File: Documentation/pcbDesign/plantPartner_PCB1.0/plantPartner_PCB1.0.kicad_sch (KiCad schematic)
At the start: 53 parts, among them IC1 MPM3610, J1 Conn_01x04, J10 Screw_Terminal, J2 Conn_01x04, J3 Conn_01x04, J4 Screw_Terminal, J5 Screw_Terminal, J6 Screw_Terminal, J7 Conn_01x03, J8 Screw_Terminal, J9 Conn_01x03, K1 SRD-05VDC-SL-C, K2 SRD-05VDC-SL-C, Q1 PNP, Q2 PNP, U1 ESP32-WROOM-32, U2 MAX485, U3 ESP32-DEVKIT-V1

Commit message: Put in the correct ESP32 (DEVKIT-V1) into Schematic. Updated the IO pin connections for ESP. Added Power supply system to SChematic. Need to update optocoupler symbol and footprint. Then routing shall commence
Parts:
- removed R22: 1k, Resistor_SMD:R_0201_0603Metric, symbol Device:R
- removed U1: ESP32-WROOM-32, RF_Module:ESP32-WROOM-32, symbol RF_Module:ESP32-WROOM-32
- added D8, D9: SS14, Diode_SMD:D_SMA, symbol Device:D_Schottky
- added J11, J16: Conn_01x04, Connector_PinHeader_2.54mm:PinHeader_1x04_P2.54mm_Vertical, symbol Connector_Generic:Conn_01x04
- added J12, J13, J14, J15: Conn_01x03, Connector_PinHeader_2.54mm:PinHeader_1x03_P2.54mm_Vertical, symbol Connector_Generic:Conn_01x03
- added J17: Barrel_Jack, Connector_BarrelJack:BarrelJack_GCT_DCJ200-10-A_Horizontal, symbol Connector:Barrel_Jack_MountingPin
- added J18: Screw_Terminal_01x02, TerminalBlock_Phoenix:TerminalBlock_Phoenix_MKDS-1,5-2-5.08_1x02_P5.08mm_Horizontal, symbol Connector:Screw_Terminal_01x02
- added R23: 1k, Resistor_SMD:R_0201_0603Metric, symbol Device:R
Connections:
- net VCC is gone; now on net 12V: IC1.2 (VCC)
- net 12V: now also U3.30 (VIN), D8.1 (K), D9.1 (K), J11.3 (Pin_3), J12.1 (Pin_1), J14.1 (Pin_1), J16.2 (Pin_2), J16.3 (Pin_3)
- net A: now also J11.2 (Pin_2)
- net ADC_LIGHT_SENSOR: now also U3.17 (VP)
- net ADC_MOISTURE_SENSOR: now also U3.18 (VN)
- net B: now also J11.1 (Pin_1)
- net COM: now also J13.2 (Pin_2), J15.2 (Pin_2)
- net DC+: now also J12.3 (Pin_3), J14.3 (Pin_3)
- net DE: now also U3.11 (D21)
- net DI: now also U3.7 (TX2)
- net EN: now also J16.4 (Pin_4)
- net FB: now also J16.1 (Pin_1)
- net GND: now also J11.4 (Pin_4), J12.2 (Pin_2), J14.2 (Pin_2), J17.2, J18.2 (Pin_2)
- net NC: now also J13.3 (Pin_3), J15.3 (Pin_3)
- net NO: now also J13.1 (Pin_1), J15.1 (Pin_1)
- net PWM_FERTIL_PIN: now also U3.28 (D13)
- net PWM_WATER_PIN: now also U3.27 (D12)
- net RO: now also R23.2
- net TEMP SWITCH: now reaches U3.20 (D35)
- net EXTERNAL LED: now reaches U3.26 (D14)
- net INTERNAL LED: now reaches U3.4 (D2)
- net at U3.6 (RX2): now also R23.1
- new net 12V_JACK: D8.2 (A), J17.1
- new net 12V_SCREW: D9.2 (A), J18.1 (Pin_1)
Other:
- note added: "ESP-32 WROOM DEVKIT V1"
- note added: "Finish testing pins for ESP32 with labels for what each Pin does. Have a stack for pins that we use and other for ones we do not."
- note added: "Power Supplies"
- note removed: "ESP-32 WROOM"
- moved on the sheet: U3

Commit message: Added the small circuitry needed for ADC sensors, ESP-32 External LED, Overall PCB Heartbeat sensor. Fixed wiring issue with 5V Relays. Met with Prof. Alex about our Alpha Build status. I tried to add new optocoupler symbol and footprint but KiCad could not find it for some reason (rip). Now I need to add used ESP-32 pins, extra 5V and 12V pins, extra GND pins, and unused ESP32 Pins, THEN finally I can route (I hope … please lol).
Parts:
- removed J17: Barrel_Jack, Connector_BarrelJack:BarrelJack_GCT_DCJ200-10-A_Horizontal, symbol Connector:Barrel_Jack_MountingPin
- removed J5, J8: Screw_Terminal, TerminalBlock_Phoenix:TerminalBlock_Phoenix_MKDS-1,5-3-5.08_1x03_P5.08mm_Horizontal, symbol Connector:Screw_Terminal_01x03
- added D10: LED, LED_SMD:LED_0201_0603Metric, symbol Device:LED
- added D11: LED, symbol Device:LED
- added J17: Conn_01x03, symbol Connector_Generic:Conn_01x03
- added J19: Barrel_Jack, Connector_BarrelJack:BarrelJack_GCT_DCJ200-10-A_Horizontal, symbol Connector:Barrel_Jack
- added J5: Conn_01x02, symbol Connector_Generic:Conn_01x02
- added R22, R24, R26: 1k, Resistor_SMD:R_0201_0603Metric, symbol Device:R
- J10, J6: value Screw_Terminal -> Screw_Terminal_01x03; footprint TerminalBlock_Phoenix:TerminalBlock_Phoenix_MKDS-1,5-3-5.08_1x03_P5.08mm_Horizontal -> (none)
- U3: footprint ESP32-DEVKIT-V1:MODULE_ESP32_DEVKIT_V1 -> MyCustomFootprints:MODULE_ESP32_DEVKIT_V1
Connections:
- net DC+ is gone; now on net 12V: J12.3 (Pin_3), J14.3 (Pin_3), J7.3 (Pin_3), J9.3 (Pin_3), Q1.3 (E), Q2.3 (E), R12.1, R14.1, R17.1, R19.1
- net PWM_FERTIL_PIN is gone; now on net 12V: U3.28 (D13)
- net PWM_WATER_PIN is gone; now on net 12V: U3.27 (D12)
- net 12V: now also J13.3 (Pin_3), J15.3 (Pin_3), K1.NC, K2.NC, J17.2 (Pin_2), J5.2 (Pin_2), R26.1
- net 12V_JACK: now also J19.1
- net ADC_LIGHT_SENSOR: now also J5.1 (Pin_1), R24.1
- net ADC_MOISTURE_SENSOR: now also J17.3 (Pin_3)
- net COM: now also J10.3 (Pin_3), J6.3 (Pin_3); no longer J10.2 (Pin_2), J6.2 (Pin_2)
- net EXTERNAL LED: now also R22.2
- net GND: now also J10.1 (Pin_1), J6.1 (Pin_1), D10.1 (K), D11.1 (K), J17.1 (Pin_1), J19.2, R24.2
- net NO: now also J10.2 (Pin_2), J6.2 (Pin_2); no longer J10.1 (Pin_1), J6.1 (Pin_1)
- removed net NC: J10.3 (Pin_3), J13.3 (Pin_3), J15.3 (Pin_3), J6.3 (Pin_3), K1.NC, K2.NC
- new net: D10.2 (A), R22.1
- new net: D11.2 (A), R26.2
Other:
- note added: "5V Relay - Fertilizer Pump"
- note added: "5V Relay - Water Pump"
- note added: "Assign Footprints to necessary LEDs/Diodes and Screw Terminals"
- note added: "Heartbeat LED"
- note added: "Pins to Add: Several 12V, 5V, and GND pins; ESP-32 Pins we are using for sensors ESP-32 Pins we are NOT using for sensors and their potential usages"
- note added: "Route PCB"
- note removed: "5V Relay - 1 of 2"
- note removed: "5V Relay - 2 of 2"
- note removed: "Verify that the imported OPTO_EL357N-G is equal to the EL354 that I have been assuming. Import all the 3D models accordingly after, add testing pins on Schematic, route PCB and add any necessary text to it"
- moved on the sheet: D8, D9, J12, J13, J14, J15, J18, R23, U3

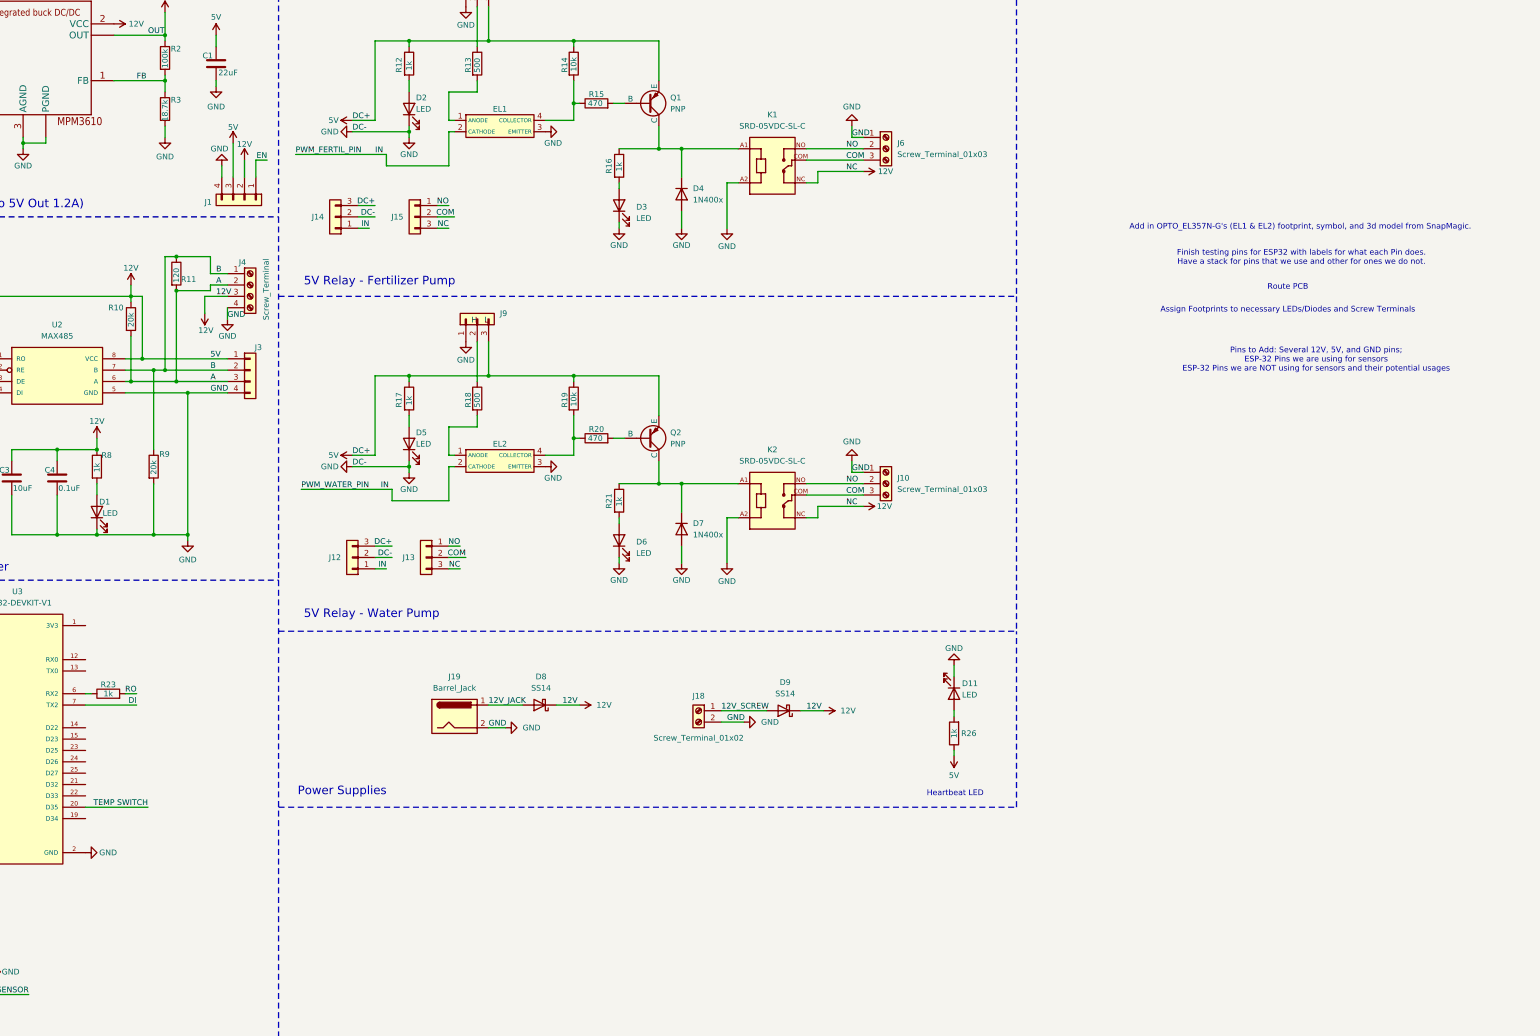
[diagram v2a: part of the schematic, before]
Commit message: Fixed optocoupler for Relay circuits
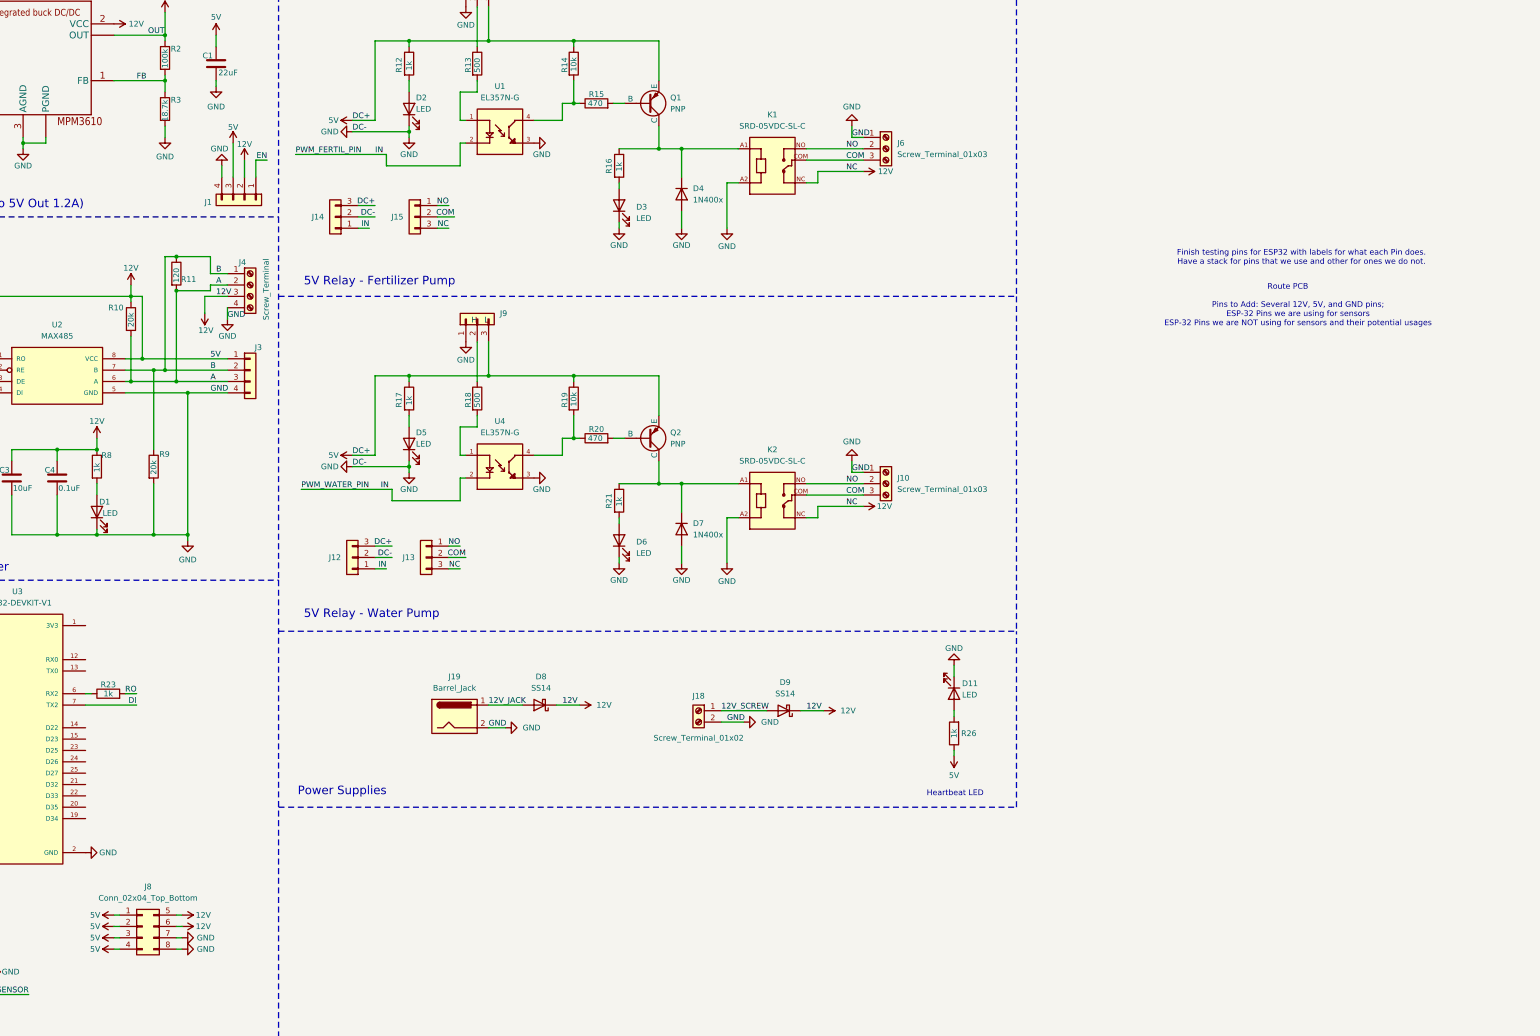
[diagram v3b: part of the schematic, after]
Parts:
- removed EL1, EL2: ~, MyCustomFootprints:OPTO_EL357N-G, symbol 12V_Relay:EL354(TA)
- added J8: Conn_02x04_Top_Bottom, Connector_PinHeader_2.54mm:PinHeader_2x04_P2.54mm_Vertical, symbol Connector_Generic:Conn_02x04_Top_Bottom
- added U1, U4: EL357N-G, MyCustomFootprints:OPTO_EL357N-G, symbol EL357N-G:EL357N-G
- D11: footprint (none) -> LED_SMD:LED_0201_0603Metric
- J10, J6: footprint (none) -> TerminalBlock_Phoenix:TerminalBlock_Phoenix_MKDS-1,5-3-5.08_1x03_P5.08mm_Horizontal
- J17: footprint (none) -> Connector_PinHeader_2.54mm:PinHeader_1x03_P2.54mm_Vertical
- J5: footprint (none) -> Connector_PinHeader_2.54mm:PinHeader_1x02_P2.54mm_Vertical
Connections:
- net 12V: now also J8.1 (Pin_1), J8.2 (Pin_2), J8.3 (Pin_3), J8.4 (Pin_4), J8.5 (Pin_5), J8.6 (Pin_6), U1.2, U4.2
- net GND: now also J8.7 (Pin_7), J8.8 (Pin_8), U1.3, U4.3
- net at R13.2: now also U1.1
- net at R14.2, R15.1: now also U1.4
- net at R19.2, R20.1: now also U4.4
- net at R18.2: now also U4.1
- net TEMP SWITCH: no longer names the net of U3.20 (D35)
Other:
- note removed: "Add in OPTO_EL357N-G's (EL1 & EL2) footprint, symbol, and 3d model from SnapMagic."
- note removed: "Assign Footprints to necessary LEDs/Diodes and Screw Terminals"

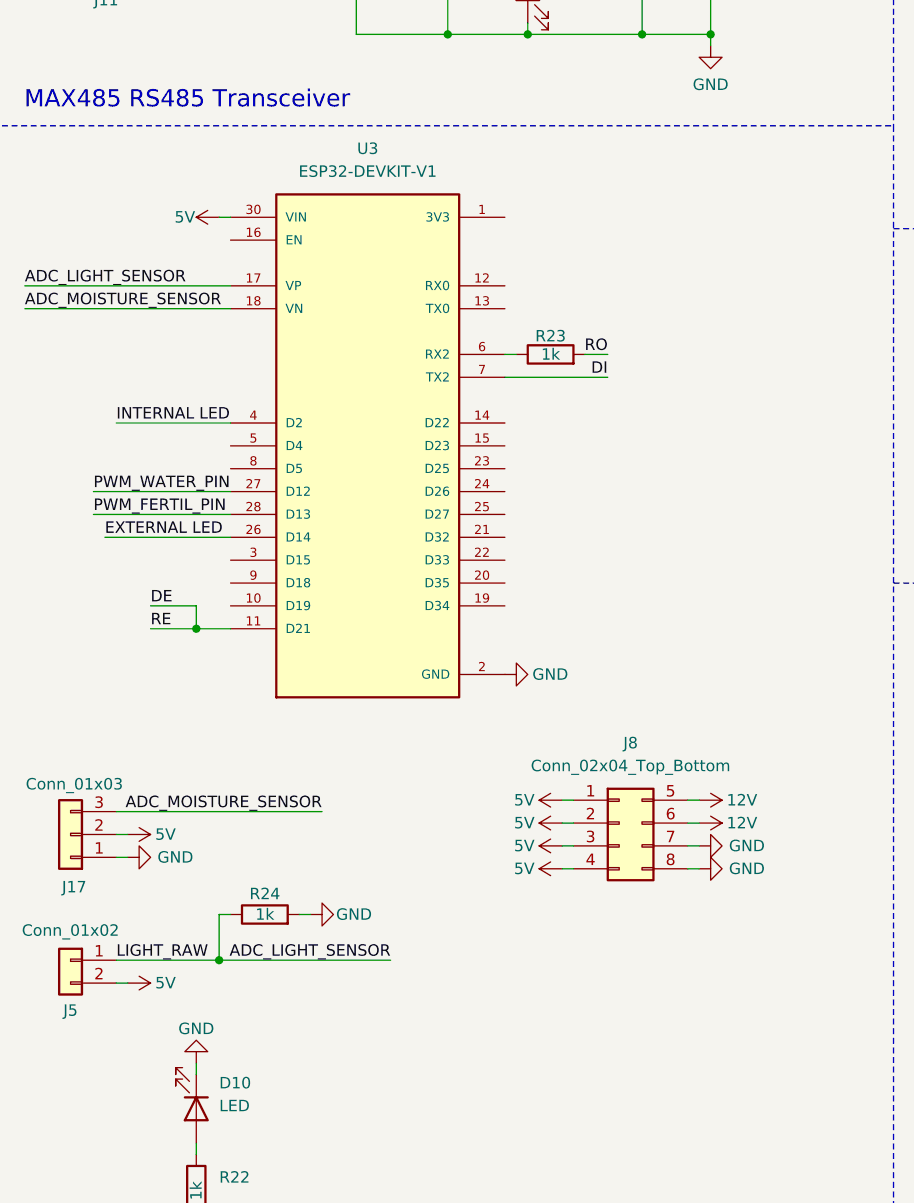
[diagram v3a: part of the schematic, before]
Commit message: Added Labels to majority of unused ESP32 Pins. I will fill in the rest later
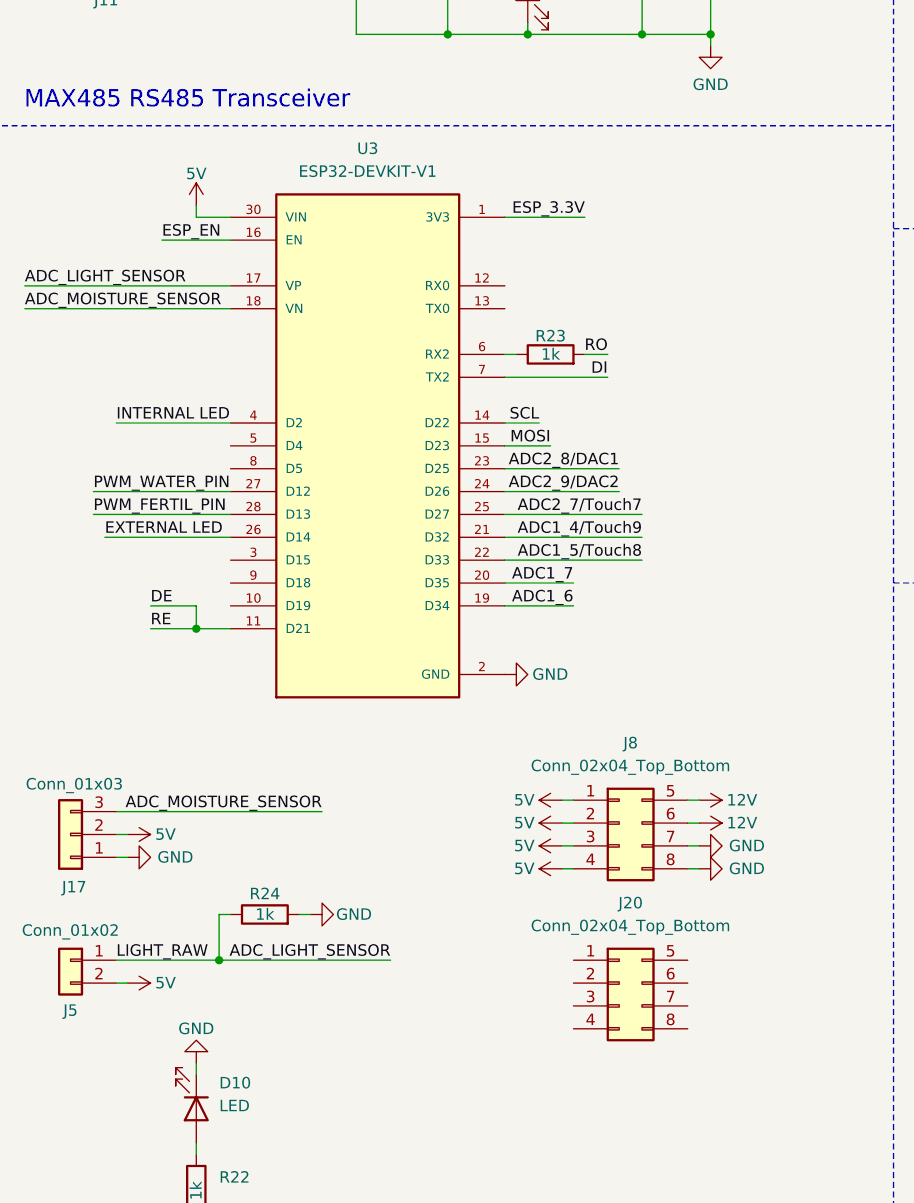
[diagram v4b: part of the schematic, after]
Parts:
- added J20: Conn_02x04_Top_Bottom, Connector_PinHeader_2.54mm:PinHeader_2x04_P2.54mm_Vertical, symbol Connector_Generic:Conn_02x04_Top_Bottom
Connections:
- net ESP_3.3V: now reaches U3.1 (3V3)
- net SCL: now reaches U3.14 (D22)
- net MOSI: now reaches U3.15 (D23)
- net ESP_EN: now reaches U3.16 (EN)
- net ADC1_6: now reaches U3.19 (D34)
- net ADC1_7: now reaches U3.20 (D35)
- net ADC1_4/Touch9: now reaches U3.21 (D32)
- net ADC1_5/Touch8: now reaches U3.22 (D33)
- net ADC2_8/DAC1: now reaches U3.23 (D25)
- net ADC2_9/DAC2: now reaches U3.24 (D26)
- net ADC2_7/Touch7: now reaches U3.25 (D27)
